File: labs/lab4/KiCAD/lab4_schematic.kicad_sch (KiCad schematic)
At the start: 18 parts, among them M1 Fan, SW1 Push Button, SW2 RotaryEncoder, U2 ATmega328P µC

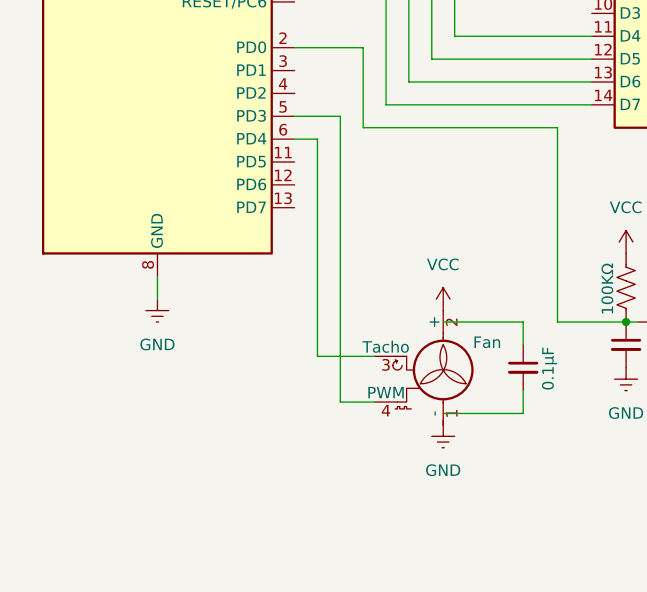
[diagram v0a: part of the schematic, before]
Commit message: added LED to the schematic
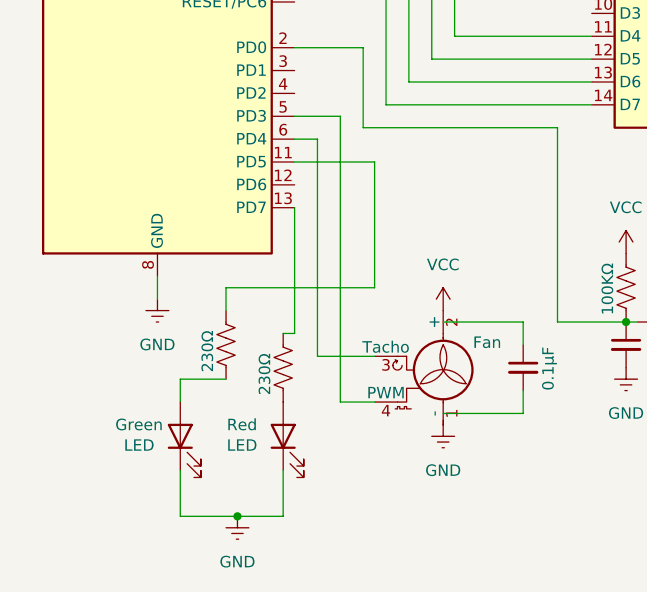
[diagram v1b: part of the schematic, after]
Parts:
- added Green, Red: LED, symbol Device:LED
- added R10, R11: 230Ω, symbol Device:R_US
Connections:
- net GND: now also Green.1 (K), Red.1 (K)
- net at U2.11 (PD5): now also R11.1
- net at U2.13 (PD7): now also R10.1
- new net: R10.2, Red.2 (A)
- new net: Green.2 (A), R11.2

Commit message: lab report work
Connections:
- net VCC: no longer M1.2 (+)
- new net Vin: M1.2 (+)
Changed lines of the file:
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@@
 		(on_board yes)
 		(dnp no)
-		(fields_autoplaced yes)
 		(property "Reference" "#PWR010"
 			(at 95.25 142.24 0)
@@
 			)
 		)
-		(property "Value" "VCC"
-			(at 95.25 133.35 0)
+		(property "Value" "Vin"
+			(at 93.726 134.62 0)
 			(effects
 				(font
 					(size 1.27 1.27)
 				)
+				(justify left)
 			)
 		)
